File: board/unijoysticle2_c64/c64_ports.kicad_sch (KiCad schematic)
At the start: 31 parts, among them J2 PORT JOY #1, J3 PORT JOY #2, SW3 MODE, SW4 SWAP, U4 74HC05, U5 74HC05, U6 74HC05

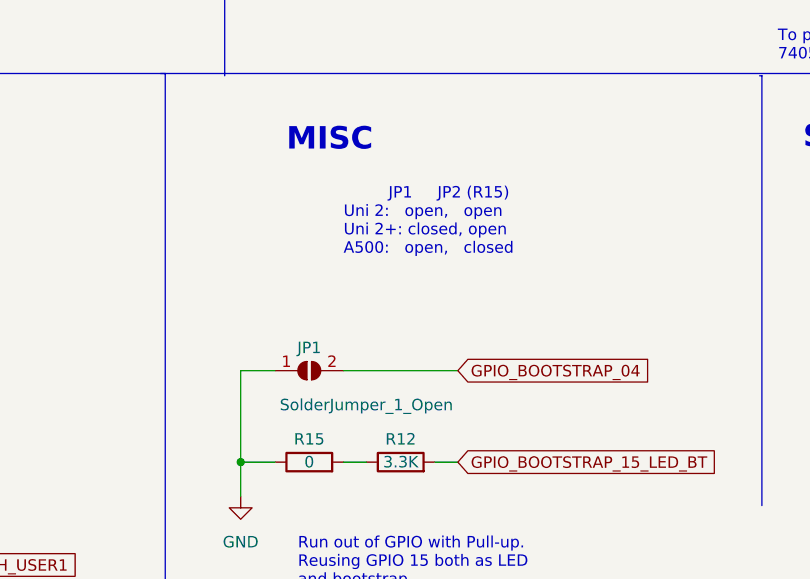
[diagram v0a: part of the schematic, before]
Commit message: c64: improved layout a bit.
board is a big larger, mounting hole better placed,
reset button moved to the left, and other layout improvements
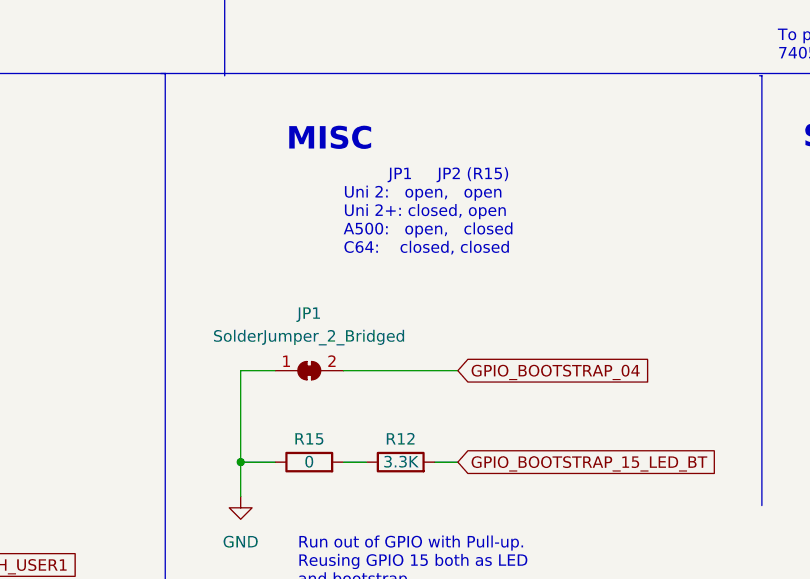
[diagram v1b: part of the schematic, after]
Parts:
- removed JP1: SolderJumper_1_Open, Jumper:SolderJumper-2_P1.3mm_Open_Pad1.0x1.5mm, symbol Jumper:SolderJumper_2_Open
- added JP1: SolderJumper_2_Bridged, Jumper:SolderJumper-2_P1.3mm_Bridged_Pad1.0x1.5mm, symbol Jumper:SolderJumper_2_Bridged
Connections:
- net GND: now also JP1.1 (A)
- net GPIO_BOOTSTRAP_04: now also JP1.2 (B)
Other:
- note added: "JP1 JP2 (R15) Uni 2: open, open Uni 2+: closed, open A500: open, closed C64: closed, closed"
- note removed: "JP1 JP2 (R15) Uni 2: open, open Uni 2+: closed, open A500: open, closed"
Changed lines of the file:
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@@
     (effects (font (size 2.4892 2.4892) (thickness 0.4978) bold) (justify left bottom))
   )
-  (text "         JP1     JP2 (R15)\nUni 2:   open,   open\nUni 2+: closed, open\nA500:   open,   closed\n"
+  (text "         JP1     JP2 (R15)\nUni 2:   open,   open\nUni 2+: closed, open\nA500:   open,   closed\nC64:    closed, closed\n"
     (at 130.81 138.43 0)
     (effects (font (size 1.27 1.27)) (justify left bottom))
@@
     (pin "7")
   )
-  (symbol (lib_id "Jumper:SolderJumper_2_Open") (at 127 151.13 0) (unit 1)
-    (in_bom yes) (on_board yes)
-    (property "Reference" "JP1" (id 0) (at 127 148.59 0))
-    (property "Value" "SolderJumper_1_Open" (id 1) (at 133.35 154.94 0))
-    (property "Footprint" "Jumper:SolderJumper-2_P1.3mm_Open_Pad1.0x1.5mm" (id 2) (at 127 151.13 0)
-      (effects (font (size 1.27 1.27)) hide)
-    )
-    (property "Datasheet" "~" (id 3) (at 127 151.13 0)
-      (effects (font (size 1.27 1.27)) hide)
-    )
-    (pin "1")
-    (pin "2")
-  )
   (symbol (lib_id "power:+3V3") (at 217.17 133.858 0) (unit 1)
     (in_bom yes) (on_board yes) (fields_autoplaced)
@@
     (pin "1")
   )
+  (symbol (lib_id "Jumper:SolderJumper_2_Bridged") (at 127 151.13 0) (unit 1)
+    (in_bom yes) (on_board yes) (fields_autoplaced)
+    (property "Reference" "JP1" (id 0) (at 127 144.78 0))
+    (property "Value" "SolderJumper_2_Bridged" (id 1) (at 127 147.32 0))
+    (property "Footprint" "Jumper:SolderJumper-2_P1.3mm_Bridged_Pad1.0x1.5mm" (id 2) (at 127 151.13 0)
+      (effects (font (size 1.27 1.27)) hide)
+    )
+    (property "Datasheet" "~" (id 3) (at 127 151.13 0)
+      (effects (font (size 1.27 1.27)) hide)
+    )
+    (pin "1")
+    (pin "2")
+  )
   (symbol (lib_id "Device:R") (at 127 161.29 90) (unit 1)

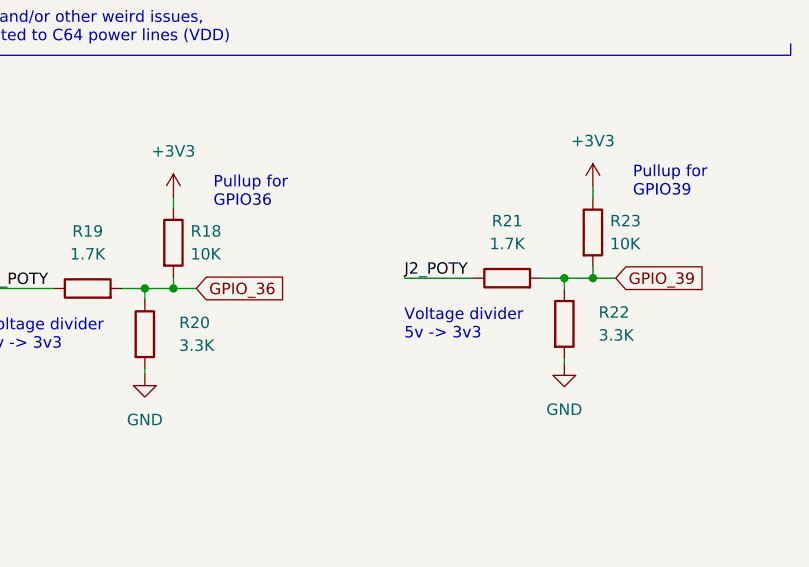
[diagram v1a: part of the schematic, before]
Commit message: c64: more progress on routing
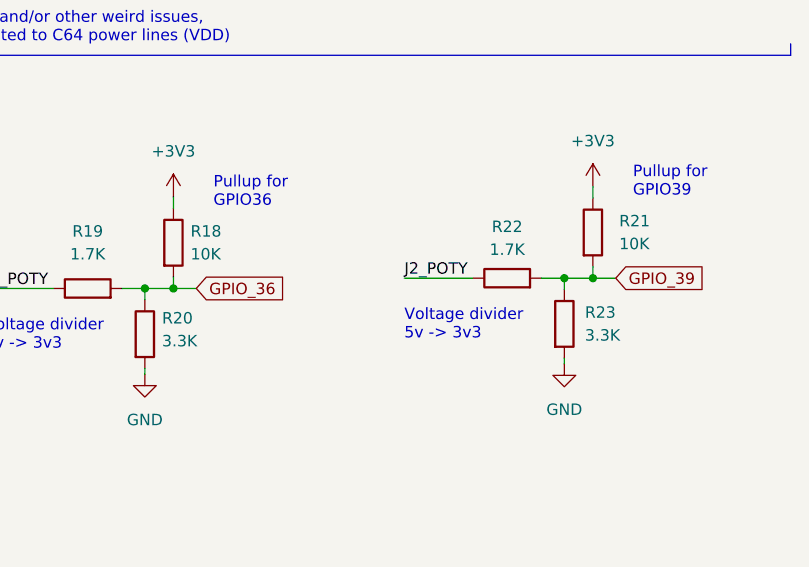
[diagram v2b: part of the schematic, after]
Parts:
- renumbered R23 to R21, R21 to R22, R22 to R23
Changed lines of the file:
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@@
   )
   (symbol (lib_id "Device:R") (at 213.995 149.098 0) (unit 1)
-    (in_bom yes) (on_board yes) (fields_autoplaced)
-    (property "Reference" "R20" (id 0) (at 217.805 147.8279 0)
-      (effects (font (size 1.27 1.27)) (justify left))
-    )
-    (property "Value" "3.3K" (id 1) (at 217.805 150.3679 0)
+    (in_bom yes) (on_board yes)
+    (property "Reference" "R20" (id 0) (at 215.9 147.32 0)
+      (effects (font (size 1.27 1.27)) (justify left))
+    )
+    (property "Value" "3.3K" (id 1) (at 215.9 149.86 0)
       (effects (font (size 1.27 1.27)) (justify left))
     )
@@
   (symbol (lib_id "Device:R") (at 260.604 147.955 0) (unit 1)
     (in_bom yes) (on_board yes) (fields_autoplaced)
-    (property "Reference" "R22" (id 0) (at 264.414 146.6849 0)
-      (effects (font (size 1.27 1.27)) (justify left))
-    )
-    (property "Value" "3.3K" (id 1) (at 264.414 149.2249 0)
+    (property "Reference" "R23" (id 0) (at 262.89 146.6849 0)
+      (effects (font (size 1.27 1.27)) (justify left))
+    )
+    (property "Value" "3.3K" (id 1) (at 262.89 149.2249 0)
       (effects (font (size 1.27 1.27)) (justify left))
     )
@@
   (symbol (lib_id "Device:R") (at 263.779 137.795 0) (unit 1)
     (in_bom yes) (on_board yes) (fields_autoplaced)
-    (property "Reference" "R23" (id 0) (at 265.684 136.5249 0)
-      (effects (font (size 1.27 1.27)) (justify left))
-    )
-    (property "Value" "10K" (id 1) (at 265.684 139.0649 0)
+    (property "Reference" "R21" (id 0) (at 266.7 136.5249 0)
+      (effects (font (size 1.27 1.27)) (justify left))
+    )
+    (property "Value" "10K" (id 1) (at 266.7 139.0649 0)
       (effects (font (size 1.27 1.27)) (justify left))
     )
@@
   (symbol (lib_id "Device:R") (at 254.254 142.875 90) (unit 1)
     (in_bom yes) (on_board yes) (fields_autoplaced)
-    (property "Reference" "R21" (id 0) (at 254.254 136.525 90))
-    (property "Value" "1.7K" (id 1) (at 254.254 139.065 90))
+    (property "Reference" "R22" (id 0) (at 254.254 137.16 90))
+    (property "Value" "1.7K" (id 1) (at 254.254 139.7 90))
     (property "Footprint" "Resistor_SMD:R_0805_2012Metric_Pad1.20x1.40mm_HandSolder" (id 2) (at 254.254 144.653 90)
       (effects (font (size 1.27 1.27)) hide)

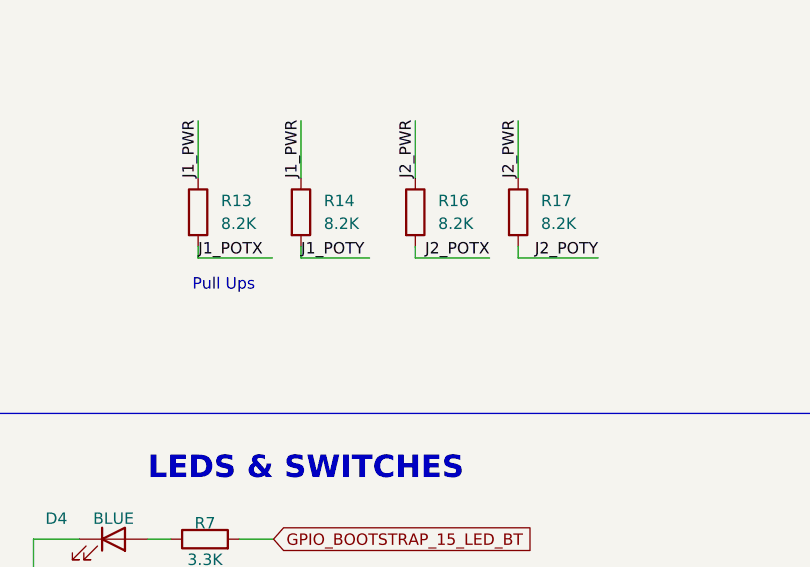
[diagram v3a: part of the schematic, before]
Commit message: c64 board: Improved description
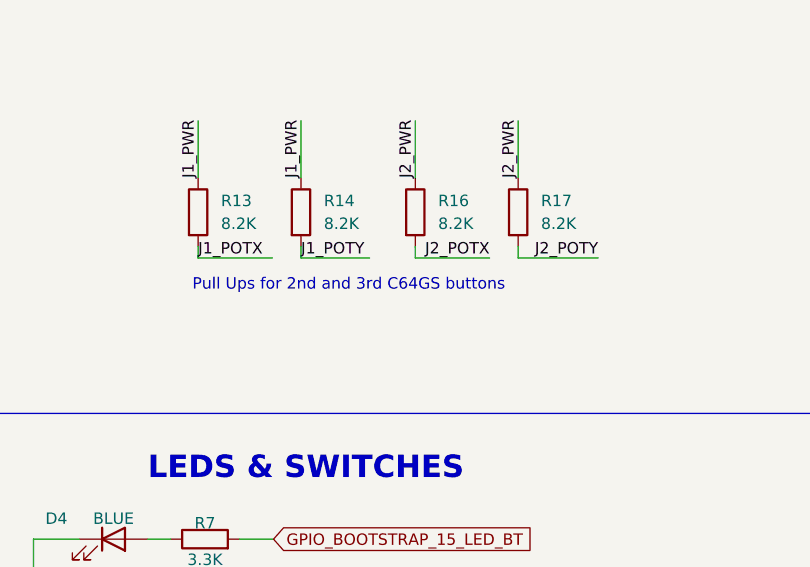
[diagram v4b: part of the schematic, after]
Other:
- note added: "Pull Ups for 2nd and 3rd C64GS buttons"
- note removed: "Pull Ups"
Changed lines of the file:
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@@
     (effects (font (size 1.27 1.27)) (justify left bottom))
   )
-  (text "Pull Ups" (at 35.433 104.648 0)
+  (text "Pull Ups for 2nd and 3rd C64GS buttons" (at 35.433 104.648 0)
     (effects (font (size 1.27 1.27)) (justify left bottom))
   )

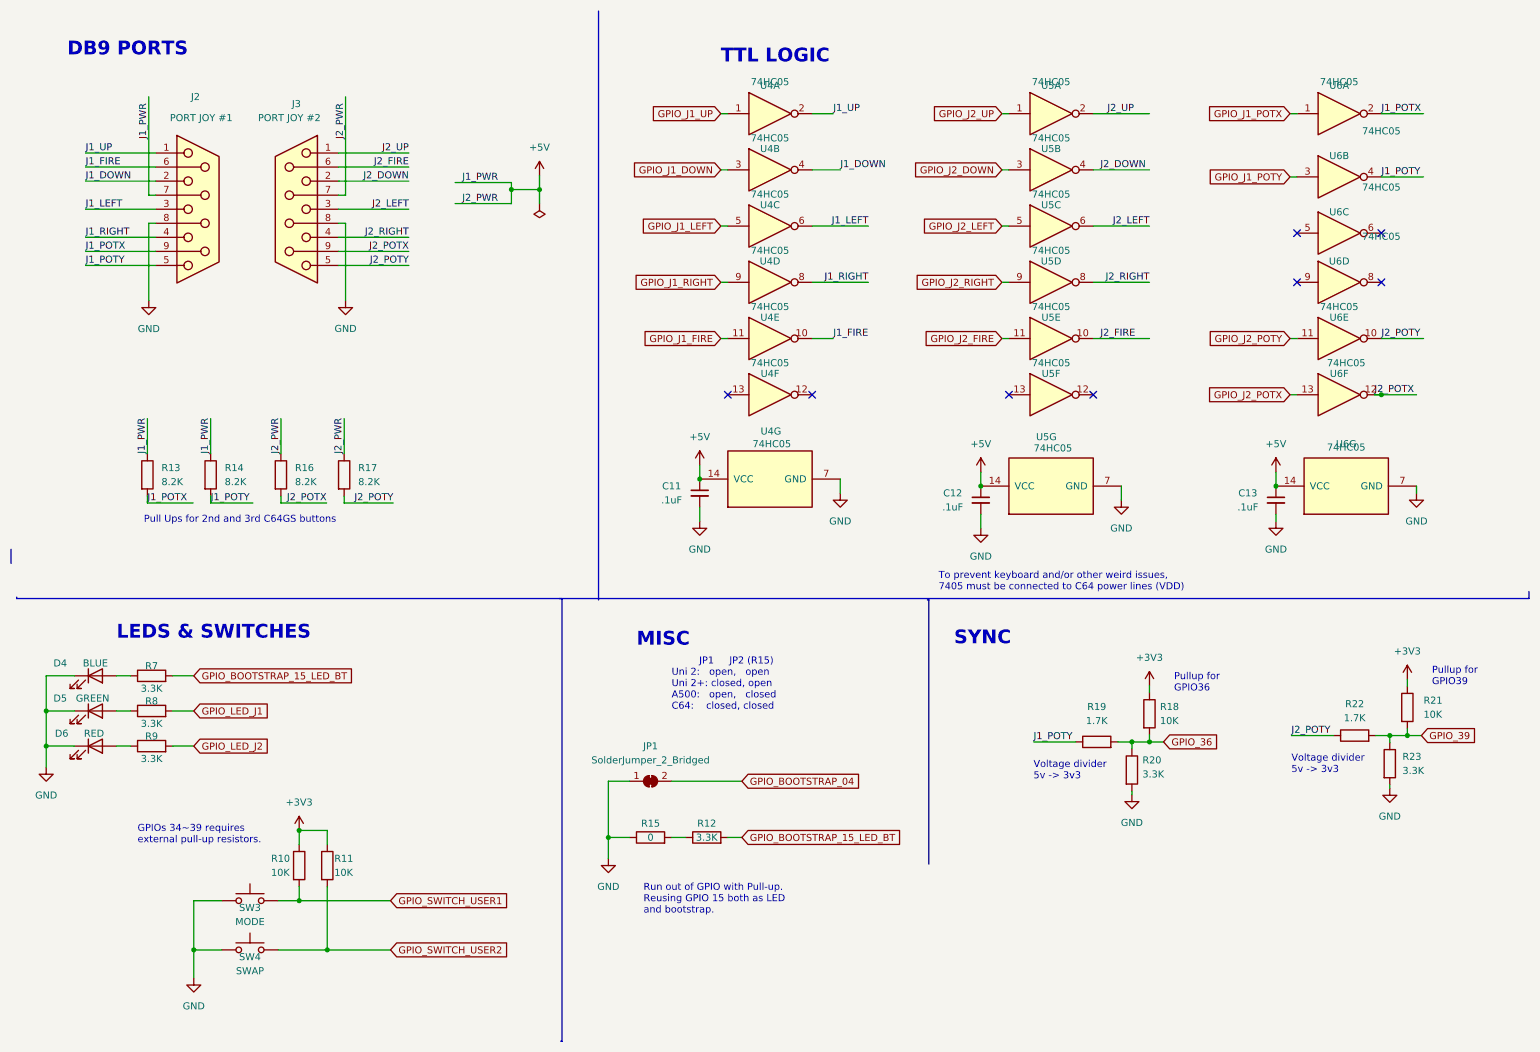
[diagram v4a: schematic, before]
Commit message: c64: rev B
Rev A had conflict with SYNC and 2nd and 3rd buttons
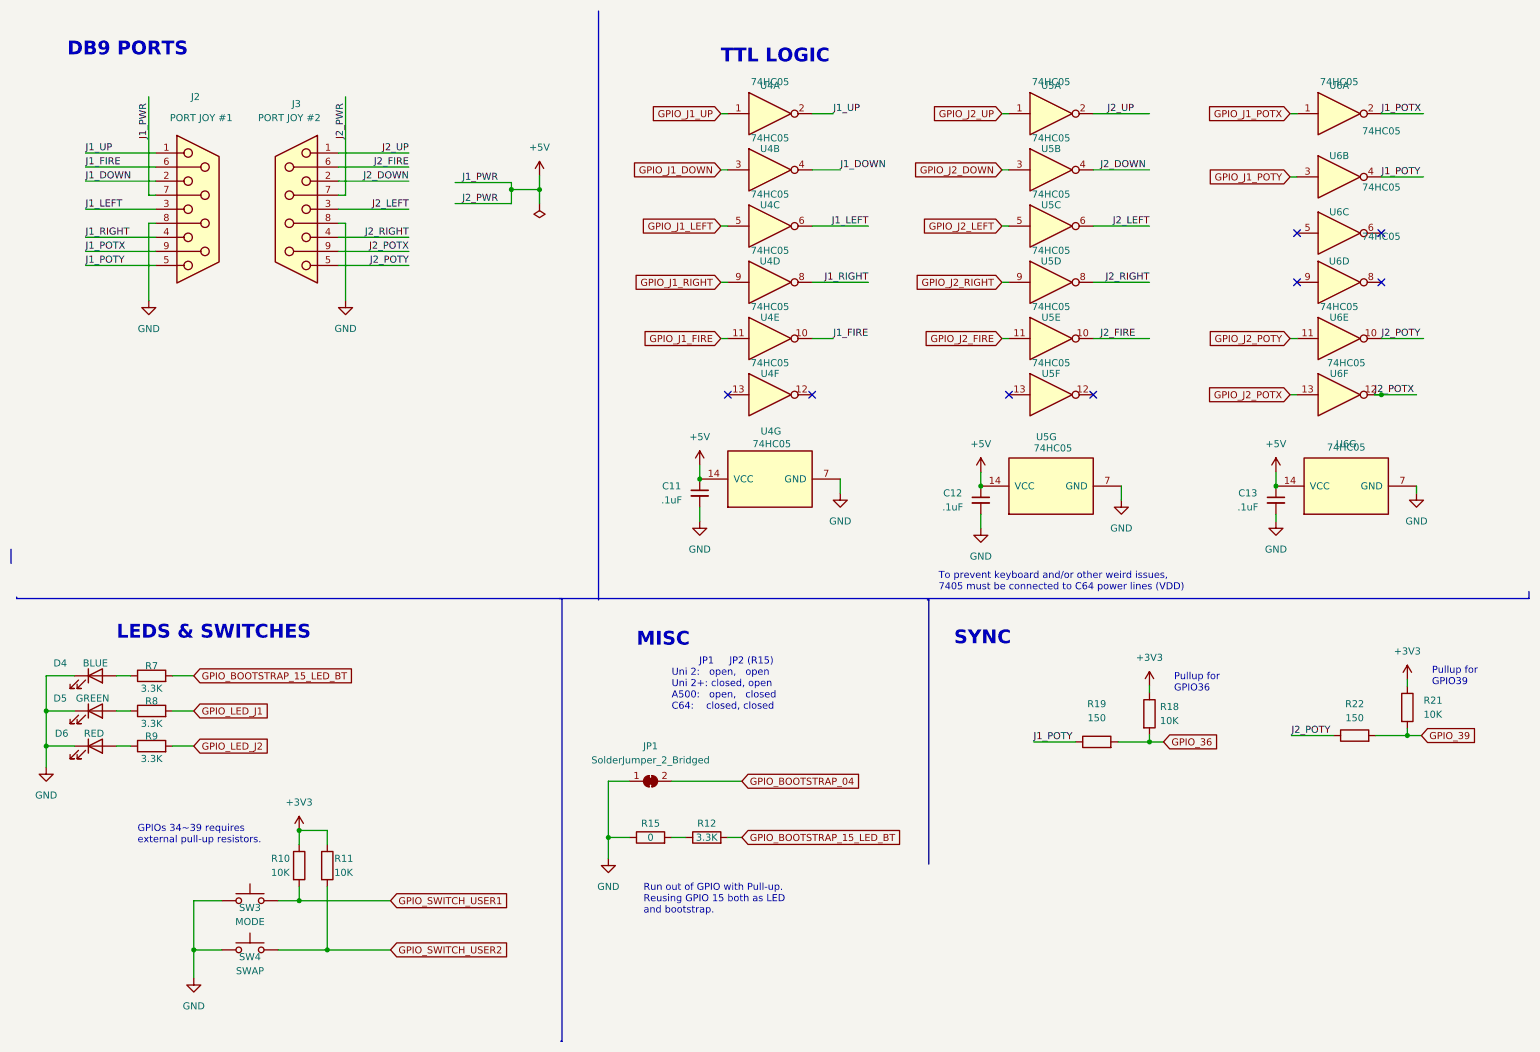
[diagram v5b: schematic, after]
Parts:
- removed R13, R14, R16, R17: 8.2K, Resistor_SMD:R_0805_2012Metric_Pad1.20x1.40mm_HandSolder, symbol Device:R
- removed R20, R23: 3.3K, Resistor_SMD:R_0805_2012Metric_Pad1.20x1.40mm_HandSolder, symbol Device:R
- R19, R22: value 1.7K -> 150
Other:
- note removed: "Pull Ups for 2nd and 3rd C64GS buttons"
- note removed: "Voltage divider 5v -> 3v3"

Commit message: flashparty / c64: remove warnings introduced in kicad 6.0.10
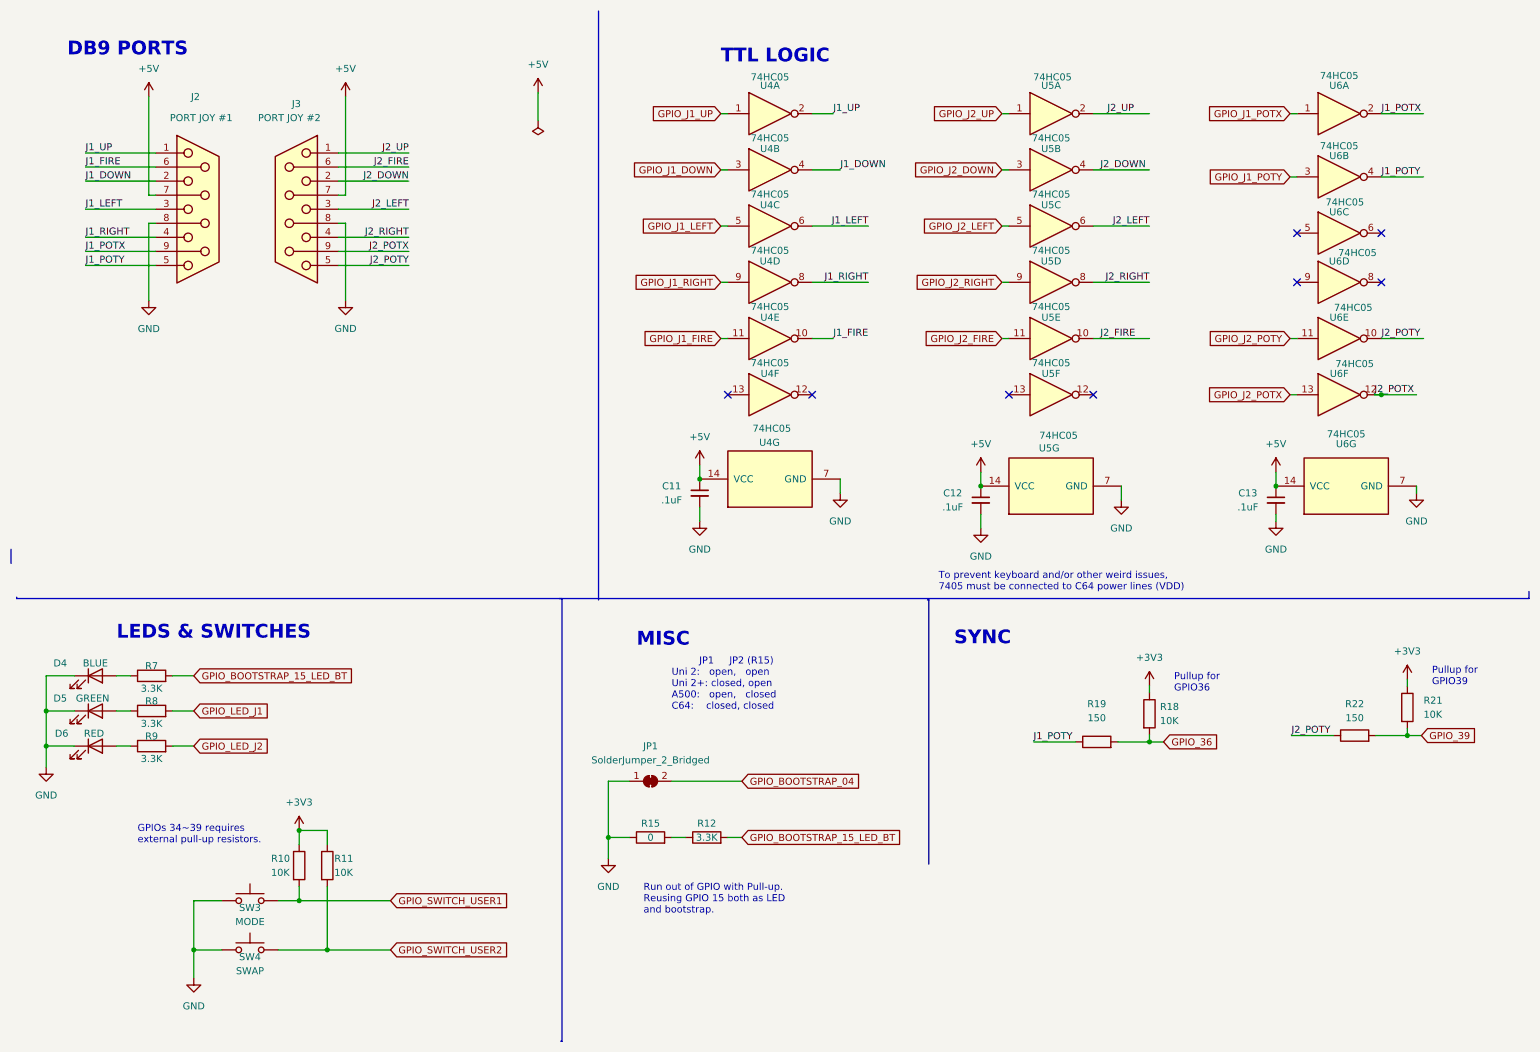
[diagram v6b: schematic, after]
